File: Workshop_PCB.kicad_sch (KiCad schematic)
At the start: 23 parts, among them J1 Conn_01x04, J2 USB_C_Receptacle_USB2.0_16P, J3 Conn_01x22, J4 Conn_01x22, SW1 SW_Push, U1 STM32F042C6Tx, U2 AMS1117-3.3, U3 USBLC6-2SC6

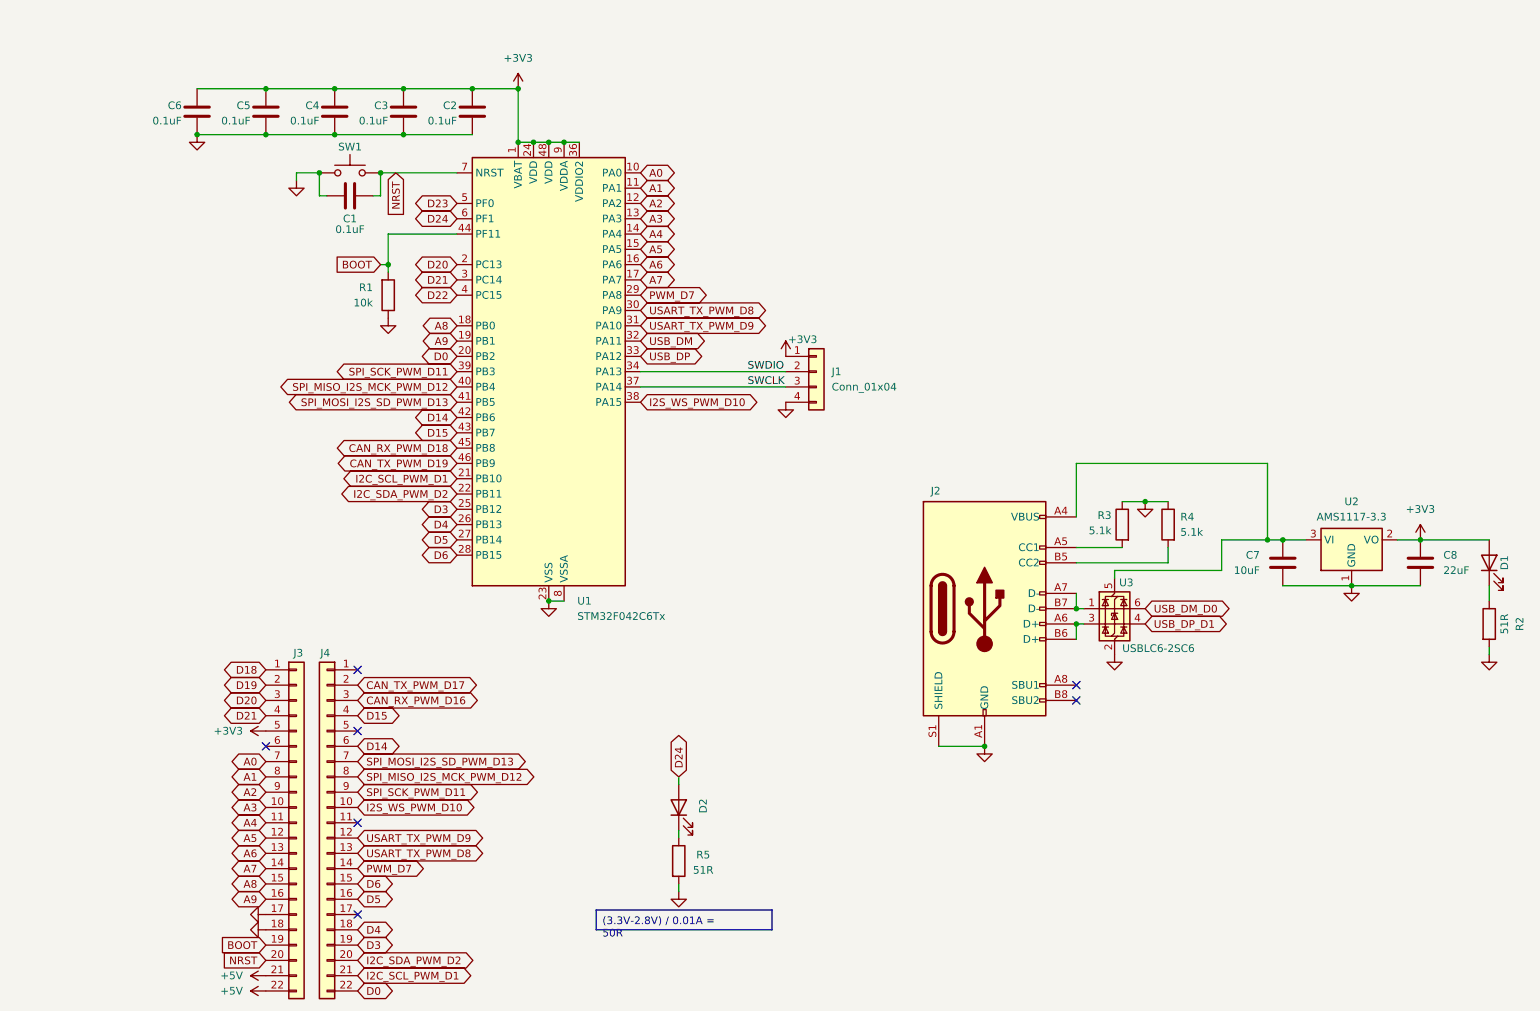
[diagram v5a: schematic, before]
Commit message: Complete fixes for PCB
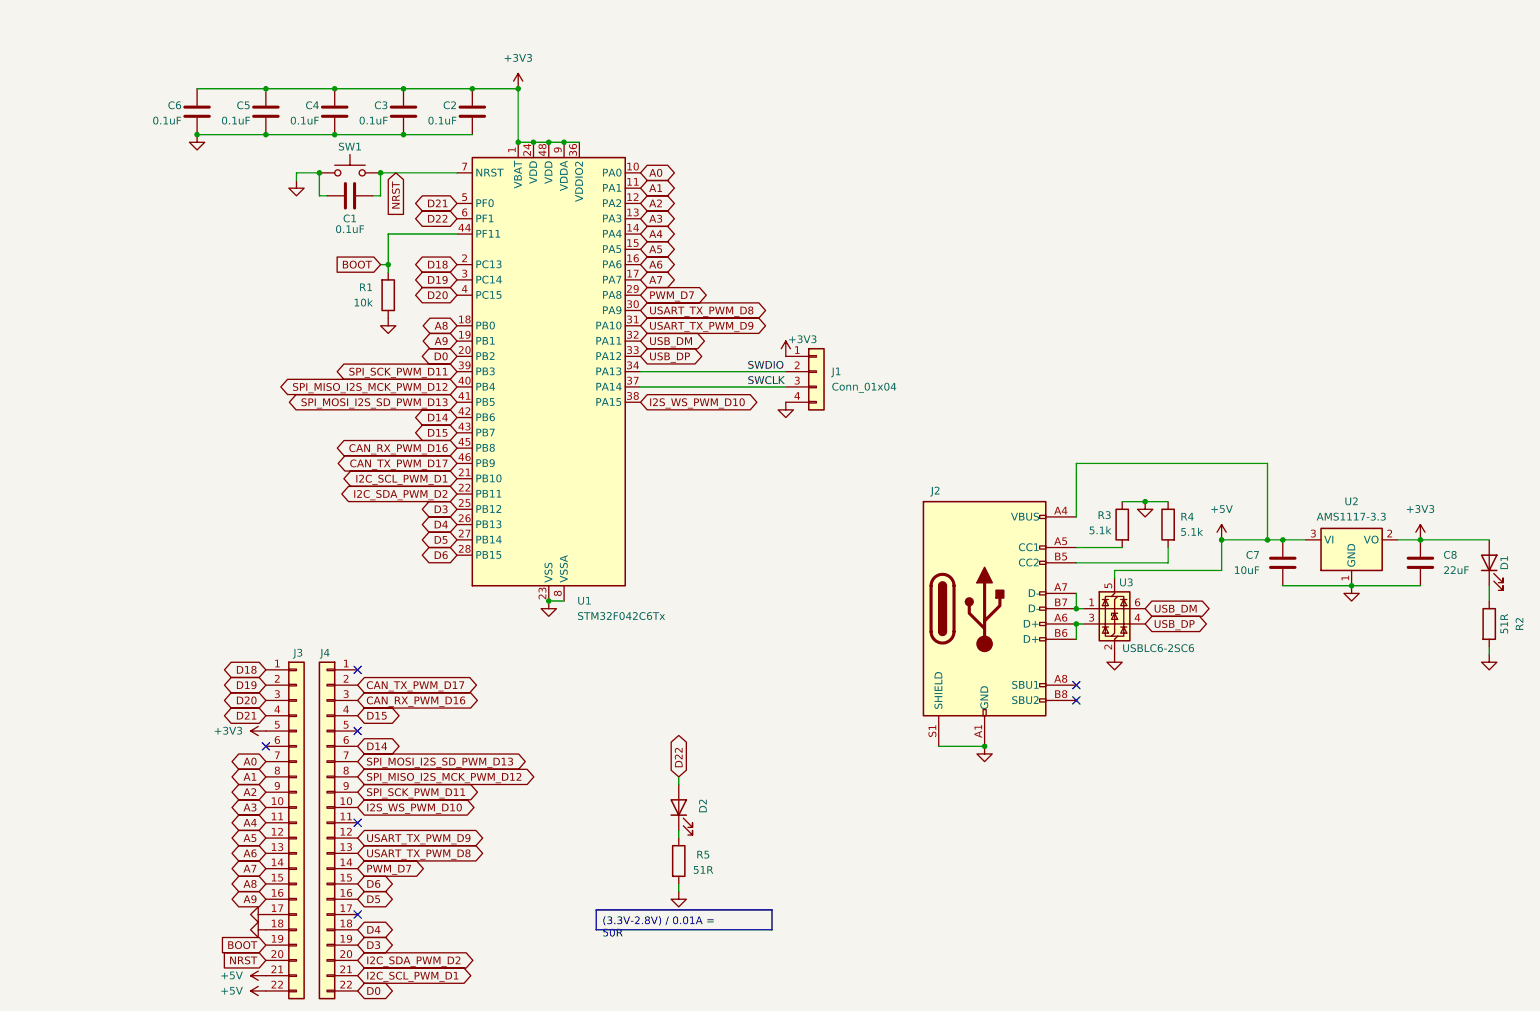
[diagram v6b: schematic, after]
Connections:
- net CAN_RX_PWM_D18 is gone; now on net CAN_RX_PWM_D16: U1.45 (PB8)
- net CAN_TX_PWM_D19 is gone; now on net CAN_TX_PWM_D17: U1.46 (PB9)
- net D23 is gone; now on net D21: U1.5 (PF0)
- net D24 is gone; now on net D22: D2.2 (A), U1.6 (PF1)
- net USB_DM_D0 is gone; now on net USB_DM: U3.6 (I/O1)
- net USB_DP_D1 is gone; now on net USB_DP: U3.4 (I/O2)
- net +5V: now also C7.1, J2.A4 (VBUS), J2.A9 (VBUS), J2.B4 (VBUS), J2.B9 (VBUS), U2.3 (VI), U3.5 (VBUS)
- net D18: now also U1.2 (PC13)
- net D19: now also U1.3 (PC14)
- net D20: now also U1.4 (PC15); no longer U1.2 (PC13)
- net D21: no longer U1.3 (PC14)
- net D22: no longer U1.4 (PC15)
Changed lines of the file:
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@@
 	)
 	(junction
+		(at 218.44 104.14)
+		(diameter 0)
+		(color 0 0 0 0)
+	)
+	(junction
 		(at 194.31 118.11)
 		(diameter 0)
@@
 		)
 	)
-	(global_label "USB_DP_D1"
+	(global_label "USB_DP"
 		(shape bidirectional)
 		(at 205.74 118.11 0)
@@
 		)
 		(property "Intersheetrefs" "${INTERSHEET_REFS}"
-			(at 220.6012 118.11 0)
+			(at 217.1541 118.11 0)
 			(effects
 				(font
@@
 		)
 	)
-	(global_label "D21"
+	(global_label "D19"
 		(shape bidirectional)
 		(at 91.44 60.96 180)
@@
 		)
 	)
-	(global_label "D24"
+	(global_label "D22"
 		(shape bidirectional)
 		(at 91.44 50.8 180)
@@
 		)
 	)
-	(global_label "USB_DM_D0"
+	(global_label "USB_DM"
 		(shape bidirectional)
 		(at 205.74 115.57 0)
@@
 		)
 		(property "Intersheetrefs" "${INTERSHEET_REFS}"
-			(at 220.7826 115.57 0)
+			(at 217.3355 115.57 0)
 			(effects
 				(font
@@
 		)
 	)
-	(global_label "CAN_RX_PWM_D18"
+	(global_label "CAN_RX_PWM_D16"
 		(shape bidirectional)
 		(at 91.44 88.9 180)
@@
 		)
 	)
-	(global_label "D23"
+	(global_label "D21"
 		(shape bidirectional)
 		(at 91.44 48.26 180)
@@
 		)
 	)
-	(global_label "D22"
+	(global_label "D20"
 		(shape bidirectional)
 		(at 91.44 63.5 180)
@@
 		)
 	)
-	(global_label "D24"
+	(global_label "D22"
 		(shape bidirectional)
 		(at 128.27 143.51 90)
@@
 		)
 	)
-	(global_label "D20"
+	(global_label "D18"
 		(shape bidirectional)
 		(at 91.44 58.42 180)
@@
 		)
 	)
-	(global_label "CAN_TX_PWM_D19"
+	(global_label "CAN_TX_PWM_D17"
 		(shape bidirectional)
 		(at 91.44 91.44 180)
@@
 					(unit 1)
 				)
+			)
+		)
+	)
+	(symbol
+		(lib_id "power:+5V")
+		(at 218.44 104.14 0)
+		(unit 1)
+		(exclude_from_sim no)
+		(in_bom yes)
+		(on_board yes)
+		(dnp no)
+		(fields_autoplaced yes)
+		(property "Reference" "#PWR011"
+			(at 218.44 107.95 0)
+			(effects
+				(font
+					(size 1.27 1.27)
+				)
+				(hide yes)
+			)
+		)
+		(property "Value" "+5V"
+			(at 218.44 99.06 0)
+			(effects
+				(font
+					(size 1.27 1.27)
+				)
+			)
+		)
+		(property "Footprint" ""
+			(at 218.44 104.14 0)
+			(effects
+				(font
+					(size 1.27 1.27)
+				)
+				(hide yes)
+			)
+		)
+		(property "Datasheet" ""
+			(at 218.44 104.14 0)
+			(effects
+				(font
+					(size 1.27 1.27)
+				)
+				(hide yes)
+			)
+		)
+		(property "Description" "Power symbol creates a global label with name \"+5V\""
+			(at 218.44 104.14 0)
+			(effects
+				(font
+					(size 1.27 1.27)
+				)
+				(hide yes)
+			)
+		)
+		(pin "1"
+		)
+		(instances
+			(project "Workshop_PCB"
+				(path "/c0781056-ba6f-4324-98d3-3fa2d5c57644"
+					(reference "#PWR011")
+					(unit 1)
+				)
